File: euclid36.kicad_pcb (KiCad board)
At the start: 2 copper layers, 88 parts, among them SW1 SW_Push, U1 ATmega32U4-AU, Y1 Crystal_GND24_Small

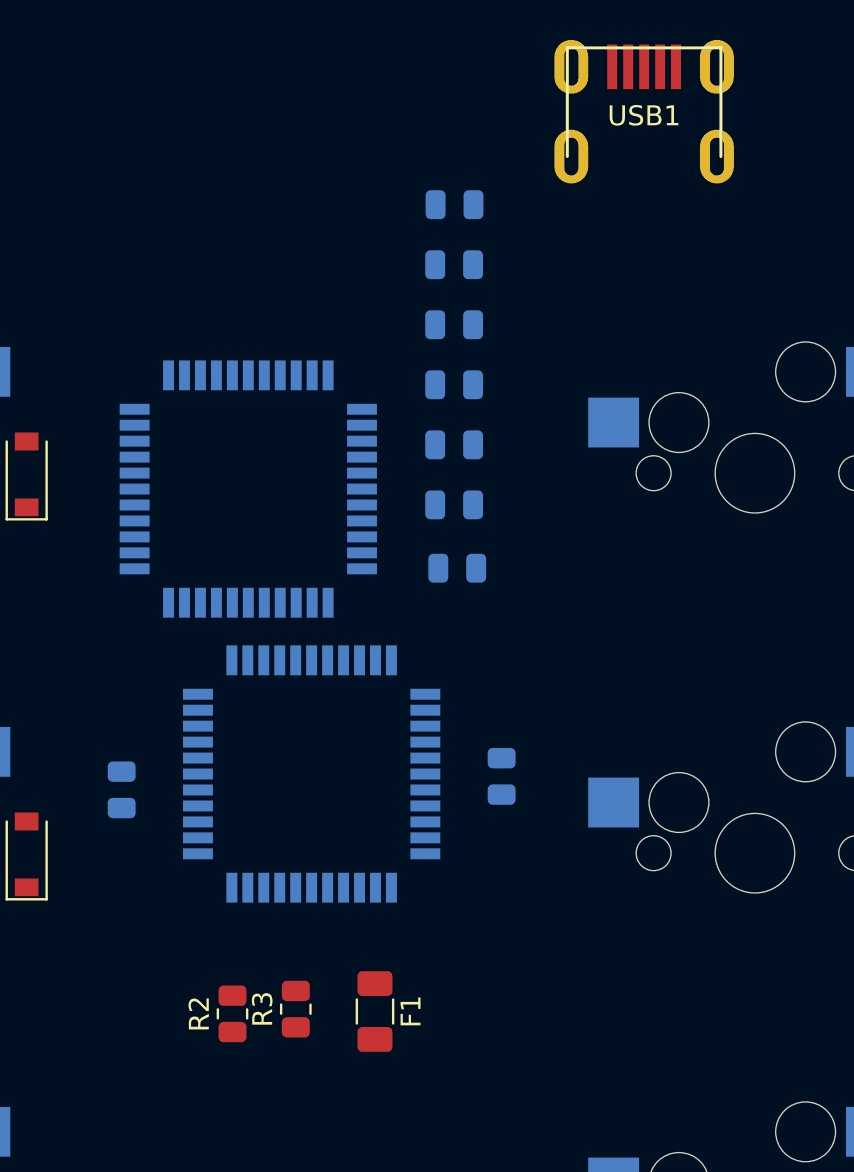
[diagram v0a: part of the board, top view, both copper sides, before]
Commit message: flipped some of the components, defined copper width for power
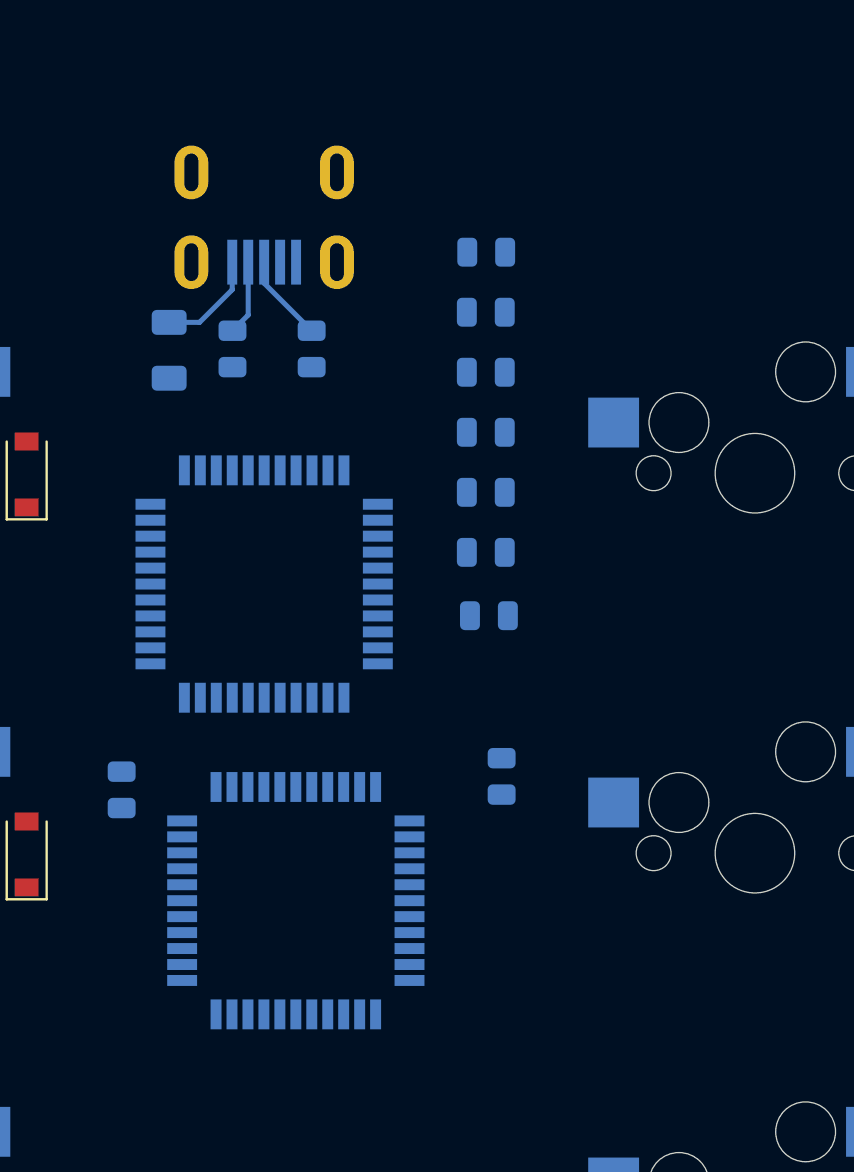
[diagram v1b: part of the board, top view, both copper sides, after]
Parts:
- F1, R2, R3, USB1: moved to B.Cu
- moved F1 34.7 mm to (144.5, 35.9), turned to 90 degrees
- moved R2 33.6 mm to (151.6, 35.8)
- moved R3 33.3 mm to (147.6, 35.8)
- moved Y1 20.8 mm to (150.8, 63.5), turned to 270 degrees
- moved USB1 19.1 mm to (149.2, 27.0), turned to 270 degrees
- moved U1 9.82 mm to (149.2, 47.6)
- moved C1 2.86 mm to (160.3, 46.0)
- moved C2 2.86 mm to (160.3, 43.0)
- moved C3 2.86 mm to (160.3, 40.0)
- moved C4 2.86 mm to (160.3, 37.0)
- moved C5 2.86 mm to (160.3, 34.0)
- moved C6 2.86 mm to (160.5, 49.2)
- moved C7 2.86 mm to (160.4, 31.0)
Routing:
- net VCC: track 0.00 -> 5.22 mm
- net D+: track 0.00 -> 4.42 mm
- net D-: track 0.00 -> 3.76 mm
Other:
- net class Default: trace_width 0.25 -> 0.254
- net class Power added: clearance 0.2, trace_width 0.381, via_dia 0.8, via_drill 0.4
